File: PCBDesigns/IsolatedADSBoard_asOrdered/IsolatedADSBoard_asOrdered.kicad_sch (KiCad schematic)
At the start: 18 parts, among them J1 Screw_Terminal_01x06, J2 Screw_Terminal_01x08, J3 Conn_01x04_MountingPin, U1 ADuM1200AR, U13 ISO1540, U14 RFM-0505S, U3 ADS1115IDGS

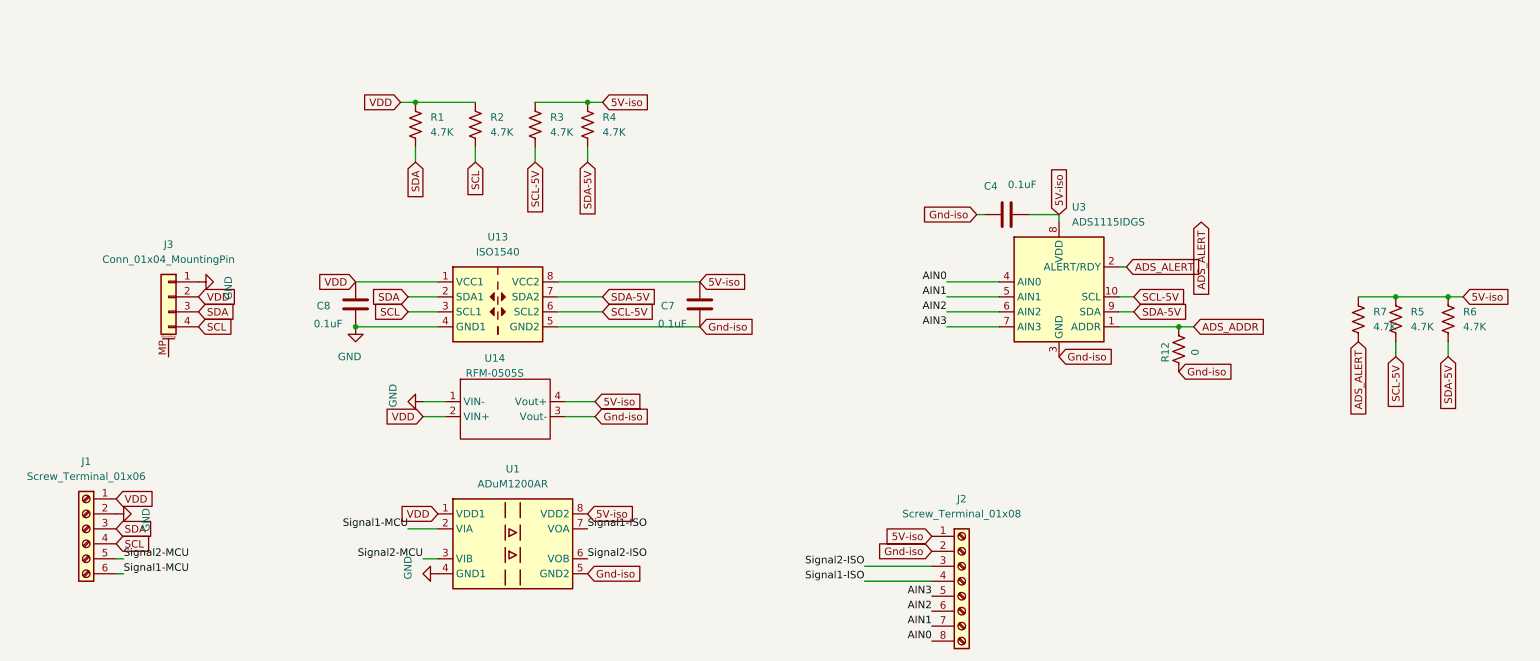
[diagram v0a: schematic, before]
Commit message: Some V2 Isolator PCB work and some radio data tests
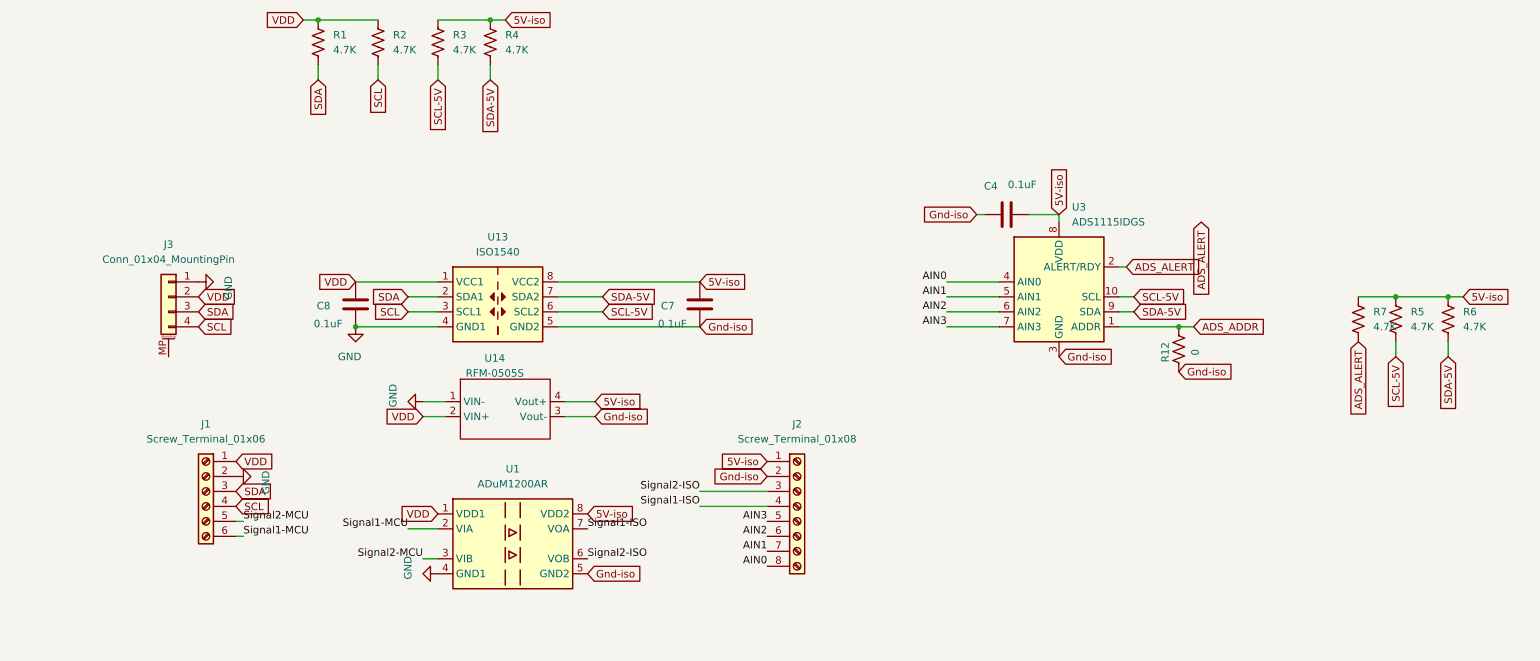
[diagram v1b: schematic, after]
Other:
- moved on the sheet: J1, J2, R1, R2, R3, R4

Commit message: Data Capture for Open Lead Detect, Swap Differential on AdaLogger
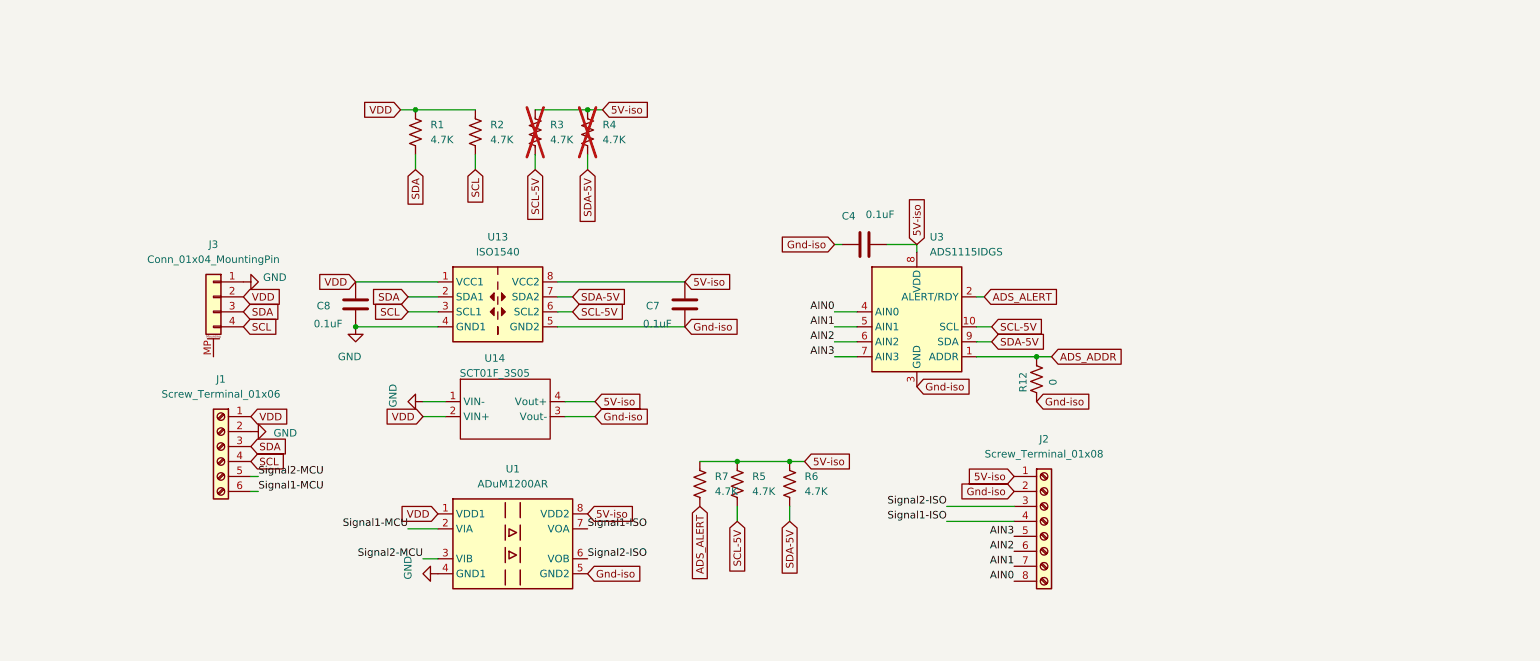
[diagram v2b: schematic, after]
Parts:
- R3, R4: now not fitted
- U14: value RFM-0505S -> SCT01F_3S05
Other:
- moved on the sheet: C4, C7, J1, J2, J3, R1, R12, R2, R5, R6, R7, U3
